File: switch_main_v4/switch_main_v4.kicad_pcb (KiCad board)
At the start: 6 copper layers, 65 x 50 mm, 468 parts, among them J2401 JST-GH-2-Horizontal, J2402 JST-GH-2-Horizontal, J2403 MSPE-J2L0-B00, J2404 MSPE-J2L0-B00, J2405 MSPE-J2L0-x00, J301 MKXS1-1 Power Input, J601 MKXS1-1 Power Input, Q1101 DMN21D2UFB-7B, Q1102 DMN21D2UFB-7B, Q1103 DMN21D2UFB-7B, Q1301 DMN21D2UFB-7B, Q1302 DMP21D0UFB-7B, Q1401 DMN21D2UFB-7B, Q1402 DMP21D0UFB-7B, Q1501 DMN21D2UFB-7B, Q1502 DMP21D0UFB-7B, Q2201 DMP21D0UFB-7B, Q2202 DMP21D0UFB-7B, Q2203 DMN21D2UFB-7B, Q2204 DMP21D0UFB-7B, Q2205 DMN21D2UFB-7B, Q2206 DMP21D0UFB-7B, Q2301 DMN21D2UFB-7B, Q2302 DMP21D0UFB-7B, Q2601 DMN21D2UFB-7B, Q2602 DMN21D2UFB-7B, Q801 DMP21D0UFB-7B, T1801 74930100, T1901 74930100, T2001 74930100, T2101 74930100, U1201 LMK1C1104DQFR, U1301 TPS62290TDRVRQ1, U1302 88Q2112-A2-NYD2A000-P123, U1401 TPS62290TDRVRQ1, U1402 88Q2112-A2-NYD2A000-P123, U1501 TPS62290TDRVRQ1, U1502 88Q2112-A2-NYD2A000-P123, U1601 LAN8671C2-E_U3B, U2201 TPS27S100BRRK, U2202 TPS27S100BRRK, U2301 NCS213RMUTAG, U2302 TPS27S100BRRK, U2501 ISO6521REUR, U2502 ISO6520REUR, U2601 STM32H503KBUx, U301 TVS3301DRBR, U302 TPS26600RHFR, U401 TPS7B8133QDRVRQ1, U402 LMQ66420MC3RXBRQ1, U403 TPS2116DRL, U501 TPS62290TDRVRQ1, U502 TPS62290TDRVRQ1, U601 TVS3301DRBR, U602 TPS26600RHFR, U701 TPS7B8133QDRVRQ1, U702 MAX20075DATCA/V+, U703 NCP508MT25TBG, U801 FM25CL64B-DG, U802 STM32H573IIKxQ, U901 SJA1105QELY, Y801 XRCGB25M000F2P02R0, Y802 ECS-.327-7-12QS-TR, Y901 XRCGB25M000F2P02R0

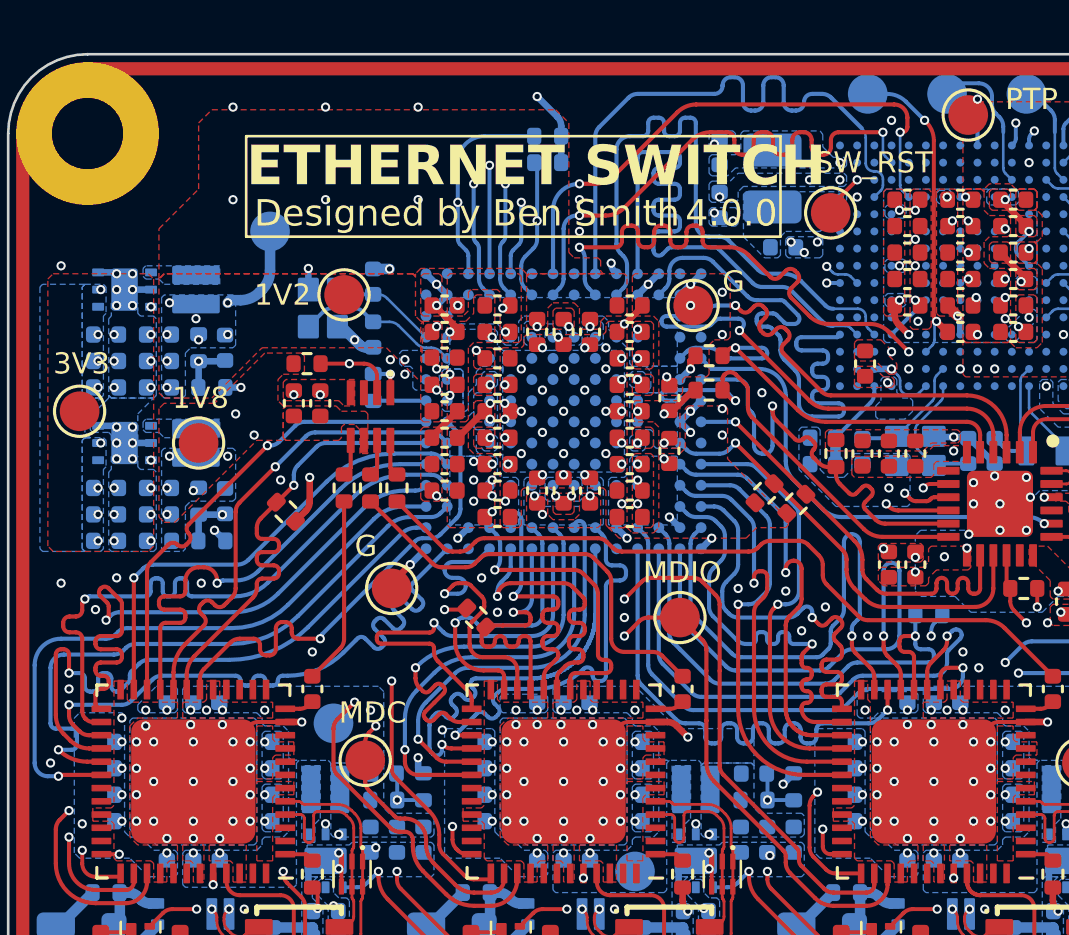
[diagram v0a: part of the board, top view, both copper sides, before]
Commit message: Fixed mistake where RMII TX and RX signals were swapped
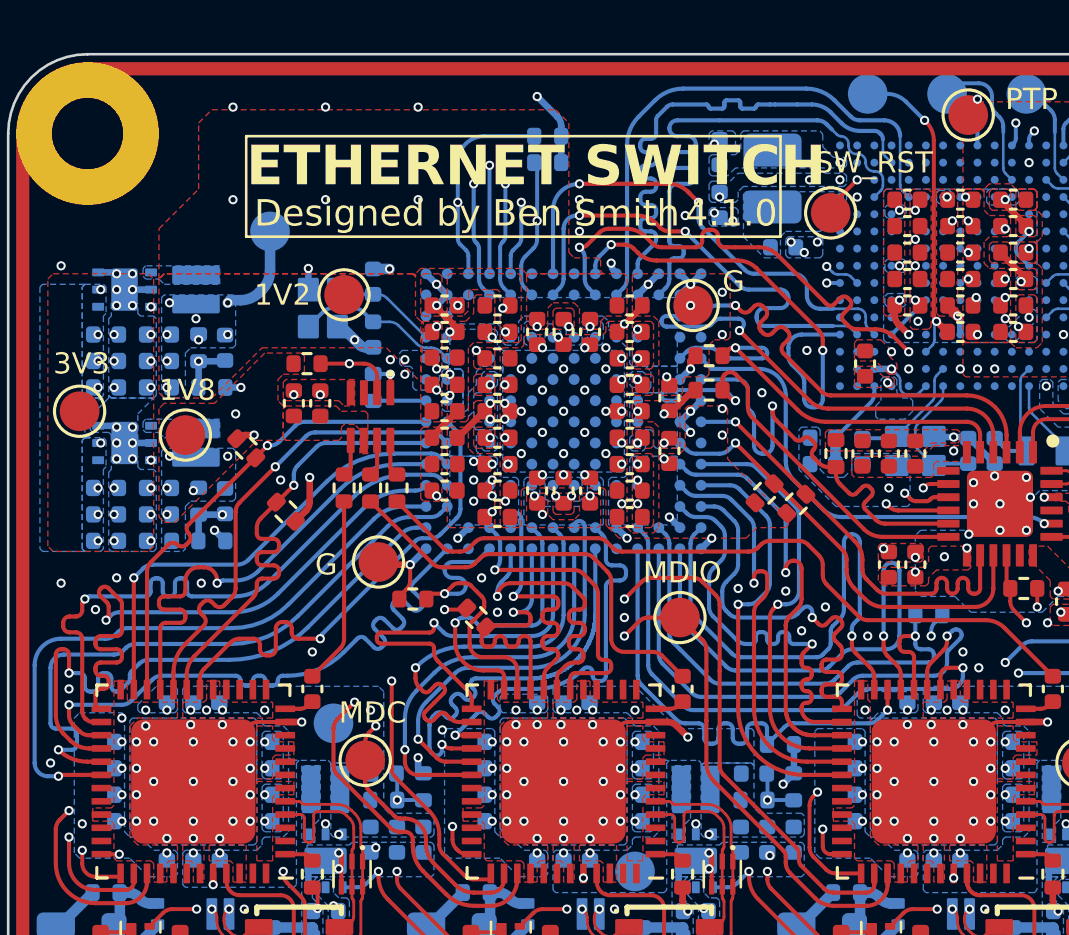
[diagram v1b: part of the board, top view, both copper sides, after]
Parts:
- added R1301: 4k7, Resistor_SMD:R_0402_1005Metric, F.Cu at (119.0, 89.9)
- added R1401: 4k7, Resistor_SMD:R_0402_1005Metric, F.Cu at (125.3, 95.6)
- added R1503: 4k7, Resistor_SMD:R_0402_1005Metric, B.Cu at (139.2, 101.1)
- moved TP1201 1.12 mm to (124.0, 94.2)
- moved TP505 0.58 mm to (116.7, 89.4)
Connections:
- U901 pad N10: /Primary MCU/RMII.RX_D0 -> /Primary MCU/RMII.TX_D0
- U901 pad N12: /Primary MCU/RMII.RX_CRS_DV -> /Primary MCU/RMII.TX_EN
- U901 pad N7: /Primary MCU/RMII.TX_D1 -> /Primary MCU/RMII.RX_D1
- U901 pad P11: /Primary MCU/RMII.RX_D1 -> /Primary MCU/RMII.TX_D1
- U901 pad P13: /Primary MCU/RMII.RX_ER -> GND1
- U901 pad P7: /Primary MCU/RMII.TX_D0 -> /Primary MCU/RMII.RX_D0
- U901 pad P9: /Primary MCU/RMII.TX_EN -> /Primary MCU/RMII.RX_CRS_DV
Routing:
- net /Primary MCU/RMII.RX_D0: track 23.1 -> 18.3 mm, vias 0 -> 2
- net /Primary MCU/RMII.RX_D1: track 23.0 -> 18.4 mm, vias 0 -> 2
- net /Primary MCU/RMII.RX_CRS_DV: track 22.8 -> 18.4 mm, vias 0 -> 2
- net GND1: track 88.9 -> 92.7 mm, vias 341 -> 343
- net /Primary MCU/RMII.TX_EN: track 23.2 -> 20.2 mm
- net /Primary MCU/RMII_REF_CLK: track 20.8 -> 18.4 mm
- net /PHYs/~{PHY1_INT}: track 54.2 -> 55.2 mm
- net /PHYs/xMII2.RX_CTL: track 20.3 -> 19.3 mm
- net /PHYs/xMII1.RX_CTL: track 11.0 -> 11.7 mm
- net /Primary MCU/RMII.TX_D0: track 21.0 -> 20.4 mm, vias 2 -> 0
- net /Primary MCU/RMII.TX_D1: track 20.9 -> 20.4 mm, vias 2 -> 0
- net +1V8: vias 52 -> 51
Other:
- board text added: "4.1.0"
- board text removed: "4.0.0"
